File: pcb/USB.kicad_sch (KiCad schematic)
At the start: 12 parts, among them J7 USB_C_Receptacle_USB2.0_16P, U11 USBLC6-2SC6, U12 TLV76133DCY

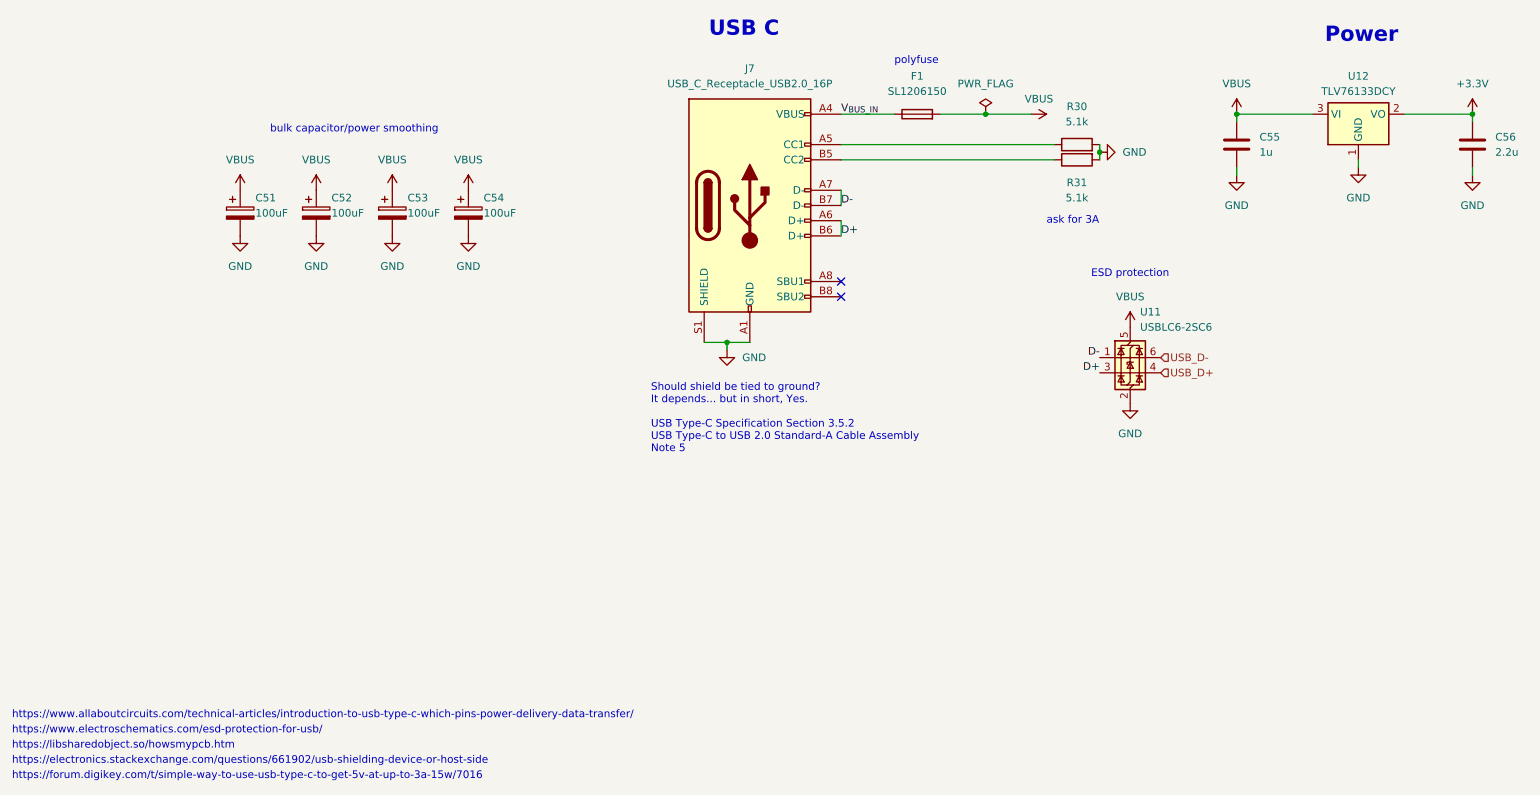
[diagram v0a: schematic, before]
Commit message: switch back to rp2350, ideal diode OR'ing for power
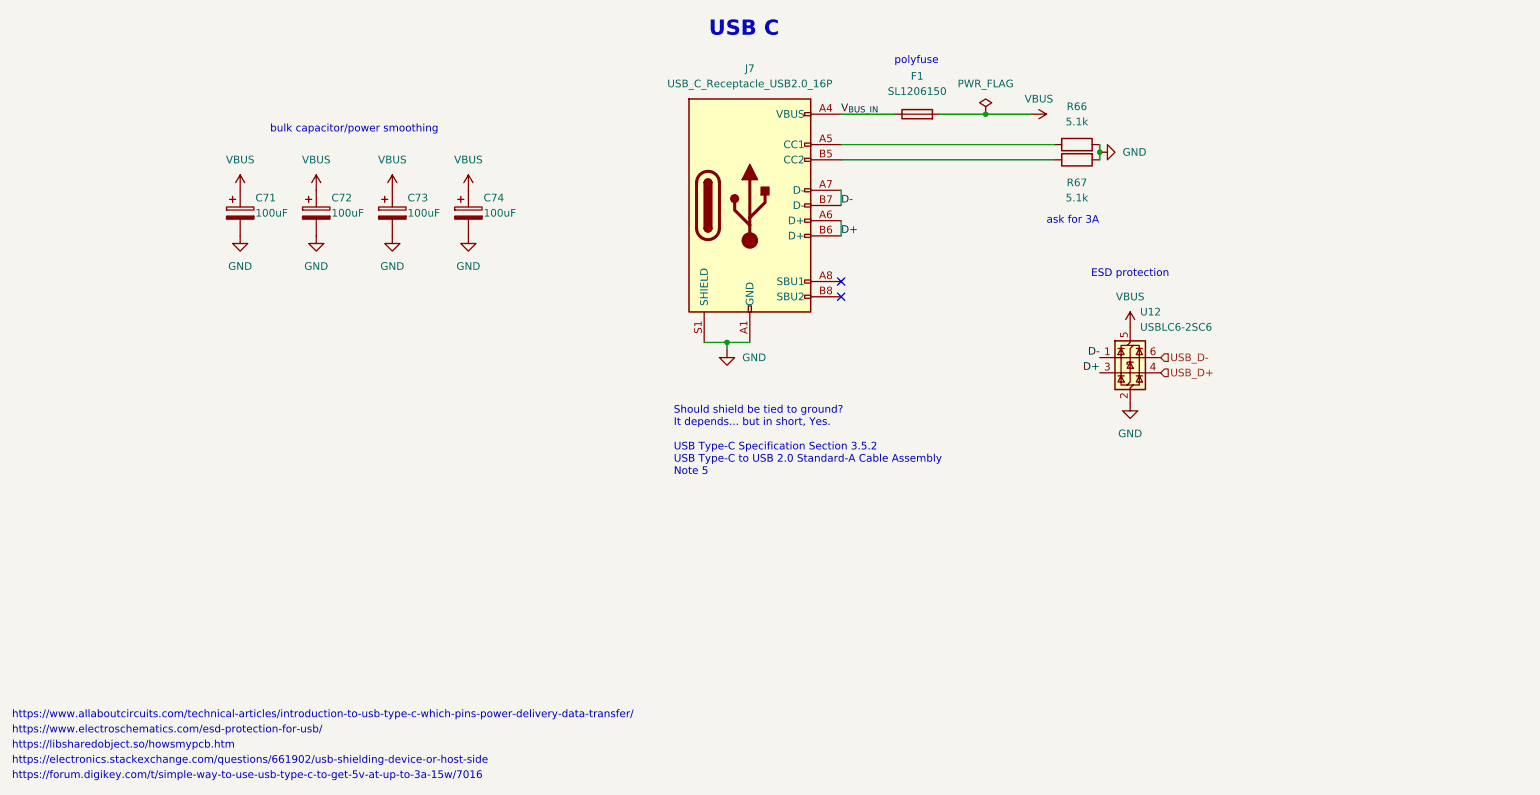
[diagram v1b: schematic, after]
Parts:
- removed C55: 1u, Capacitor_SMD:CP_Elec_4x3, symbol Device:C
- removed C56: 2.2u, Capacitor_SMD:CP_Elec_4x3, symbol Device:C
- removed U12: TLV76133DCY, Package_TO_SOT_SMD:SOT-223-3_TabPin2, symbol Regulator_Linear:TLV76133DCY
- renumbered C51 to C71, C52 to C72, C53 to C73, C54 to C74, R30 to R66, R31 to R67, U11 to U12
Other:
- note removed: "Power"
